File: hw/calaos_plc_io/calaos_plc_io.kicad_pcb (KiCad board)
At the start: 2 copper layers, 100.3 x 93.2 mm, 223 parts, among them P1 CONN_01X03, P2 CONN_01X06, P3 CONN_01X20, P4 CONN_01X20, P5 SERIAL_DBG, Q1 Q_NPN_BCE, Q10 Q_NPN_BCE, Q11 Q_NPN_BCE, Q12 Q_NPN_BCE, Q13 Q_NPN_BCE, Q14 Q_NPN_BCE, Q15 Q_NPN_BCE, Q16 Q_NPN_BCE, Q17 Q_NPN_BCE, Q18 Q_NPN_BCE, Q19 Q_NPN_BCE, Q2 Q_NPN_BCE, Q20 Q_NPN_BCE, Q3 Q_NPN_BCE, Q4 Q_NPN_BCE, Q5 Q_NPN_BCE, Q6 Q_NPN_BCE, Q7 Q_NPN_BCE, Q8 Q_NPN_BCE, Q9 Q_NPN_BCE, U1 LM7824CT, U10 LTV-847, U11 LTV-847, U12 LTV-847, U13 LTV-847, U14 LTV-847, U15 LTV-847, U16 LTV-847, U2 LM7805CT, U3 LTV-847, U4 LD1117S33TR, U5 MAX485, U6 STM32F030K6, U7 PCA9505, U8 LTV-847, U9 LTV-847, Y1 8MHz

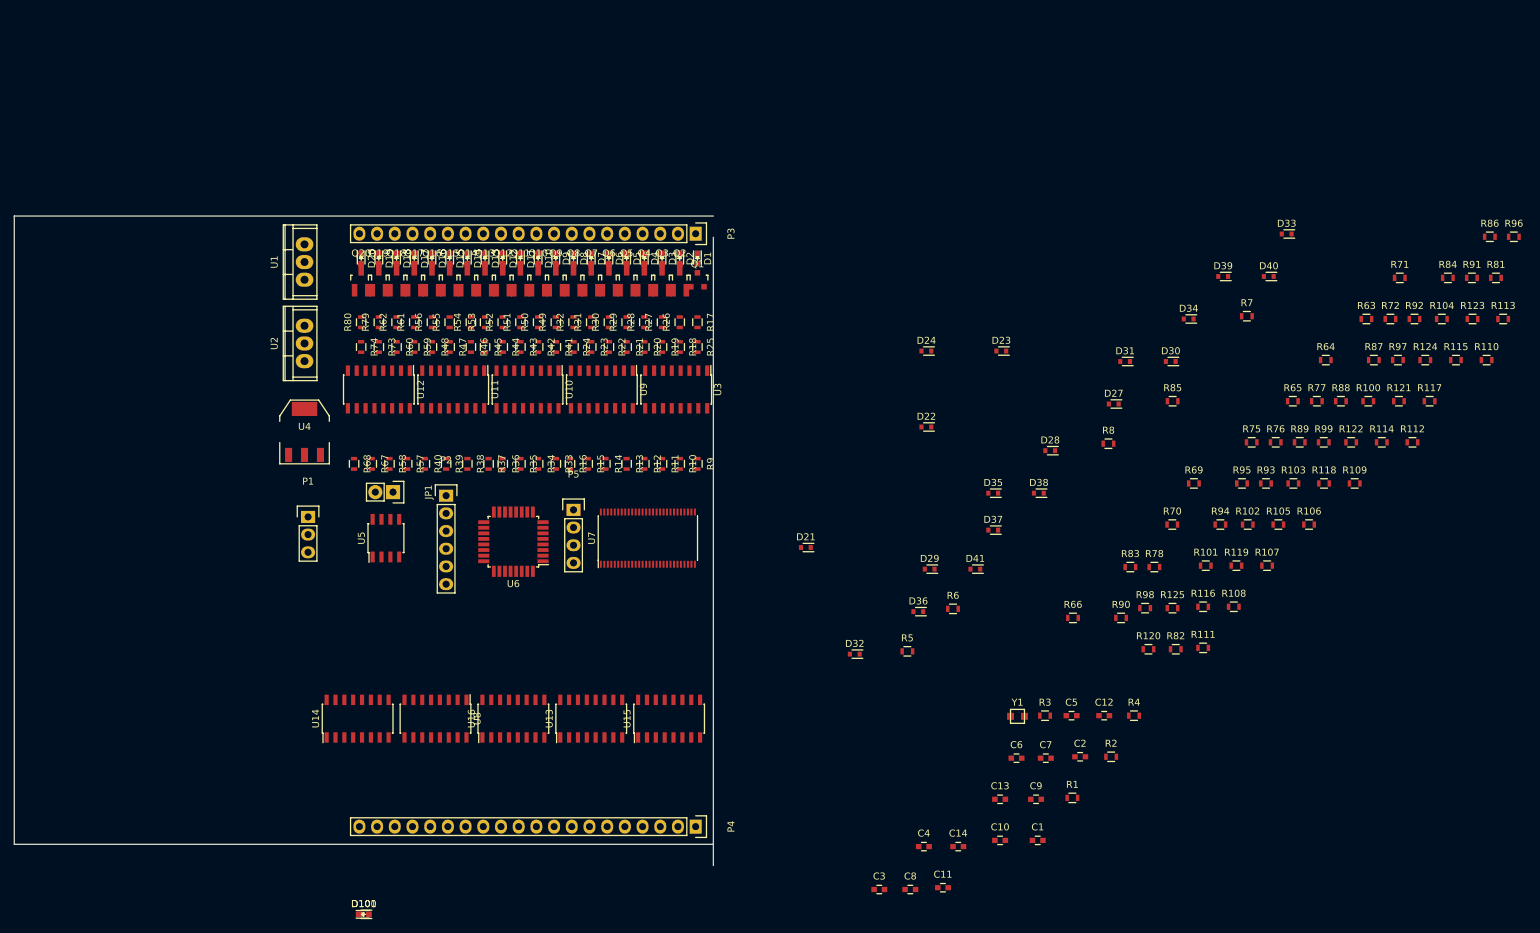
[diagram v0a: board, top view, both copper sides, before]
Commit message: Add pcb with placement of components
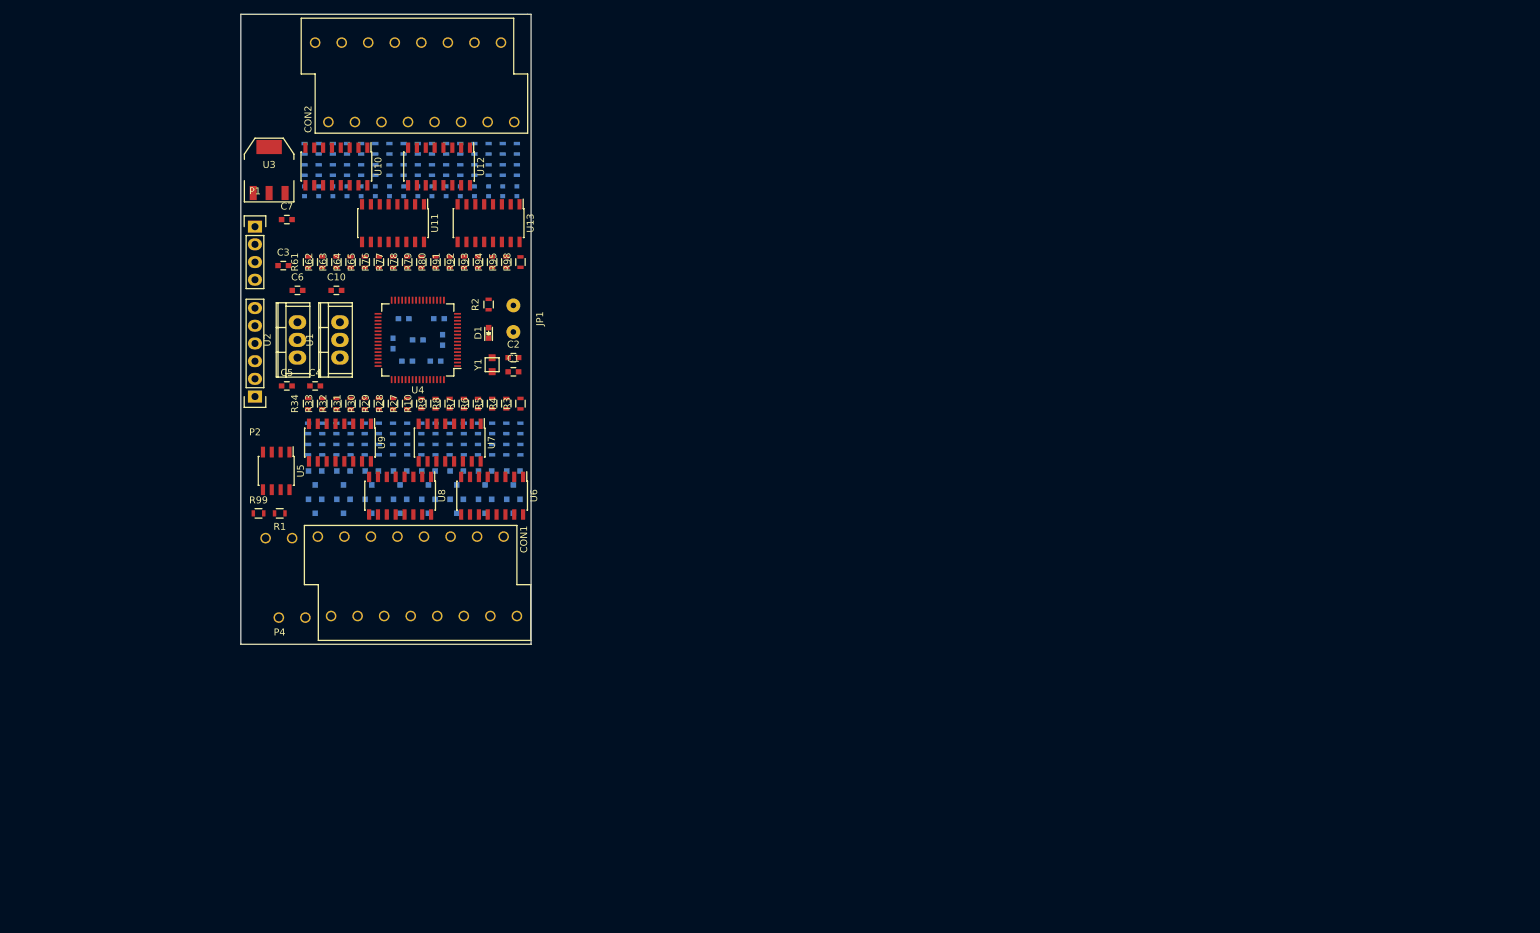
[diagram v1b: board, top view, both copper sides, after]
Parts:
- removed D10, D100, D11, D12, D13, D14, D15, D16, D17, D2, D3, D4, D5, D6, D7, D8, D9: LED, LEDs:LED-0603
- removed D101, D34, D35, D36, D37, D38, D39, D40, D41: TVS 3v3, Diodes_SMD:SOD-523
- removed P3: CONN_01X20, Pin_Headers:Pin_Header_Straight_1x20
- removed P5: SERIAL_DBG, Pin_Headers:Pin_Header_Straight_1x04
- removed Q17, Q18, Q19, Q20: Q_NPN_BCE, Housings_SOT-23_SOT-143_TSOT-6:SOT-23_Handsoldering
- removed R100, R101, R102, R103, R104, R105, R111, R112, R113, R114, R115, R116, R117, R118, R119, R120: 390, Resistors_SMD:R_0603
- removed R106, R107, R108, R109, R110, R121, R122, R123, R124, R125: 10k, Resistors_SMD:R_0603
- removed U14, U15, U16: LTV-847, Housings_SOIC:SOIC-16_3.9x9.9mm_Pitch1.27mm
- added C15: 100nF, Capacitors_SMD:C_0603, B.Cu at (149.4, 94.0)
- added CON1: TerminalBlock, plc:Terminalblock_1708084, F.Cu at (163.6, 133.6)
- added CON2: TerminalBlock, plc:Terminalblock_1708084, F.Cu at (134.6, 51.3)
- added D25: TVS 3v3, Diodes_SMD:SOD-523, B.Cu at (147.3, 72.6)
- added D26: TVS 3v3, Diodes_SMD:SOD-523, B.Cu at (149.4, 72.6)
- C1, C2: value 0.33uF -> 20pF
- C10: value 100nF -> 10uF
- C11, C12, C13, C14, C9, D21, D22, D23, D24, D27, D28, D29, D30, D31, D32, D33, Q1, R17, R18, R19, R20, R21, R22, R23, R24, R25, R26, R41, R42, R43, R44, R45, R46, R47, R48, R49, R50, R66, R69, R70, R71, R72, R81, R82, R83, R84, R85, R86, R87, R88, R89, R90, R96, R97: moved to B.Cu
- C3, C4: value 0.1uF -> 0.33uF
- C5, C6: value 20pF -> 0.1uF
- C8: value 10uF -> 100nF; moved to B.Cu
- D18, D19, D20: value LED -> TVS 3v3; footprint LEDs:LED-0603 -> Diodes_SMD:SOD-523; moved to B.Cu
- JP1: value JUMPER -> Jumper_NO_Small; footprint Pin_Headers:Pin_Header_Straight_1x02 -> Wire_Pads:SolderWirePad_2x_0-8mmDrill
- P1: value CONN_01X03 -> SERIAL_DBG; footprint Pin_Headers:Pin_Header_Straight_1x03 -> Pin_Headers:Pin_Header_Straight_1x04
- P4: value CONN_01X20 -> CONN_01X04; footprint Pin_Headers:Pin_Header_Straight_1x20 -> plc:Terminalbloc_1726040
- Q10, Q11, Q12, Q13, Q14, Q15, Q16, Q2, Q3, Q4, Q5, Q6, Q7, Q8, Q9: footprint Housings_SOT-23_SOT-143_TSOT-6:SOT-23_Handsoldering -> Housings_SOT-23_SOT-143_TSOT-6:SOT-23; moved to B.Cu
- R1: value 120 -> 1k
- R11, R12, R13, R14, R15, R16, R35, R36, R37, R38, R39, R40: value 220 -> 10k; moved to B.Cu
- R2: value 10k -> 510
- R27, R28, R29, R30, R31, R32, R7, R8: value 10k -> 220
- R3, R4: value 510 -> 220
- R5, R6: value 390 -> 220
- R51, R52, R53, R54, R55, R56, R59, R60, R73, R74, R75: value 10k -> 390; moved to B.Cu
- R57, R58, R67, R68: value 220 -> 390; moved to B.Cu
- R63, R64, R65, R98: value 390 -> 10k
- R99: value 390 -> 120
- U3: value LTV-847 -> LD1117S33TR; footprint Housings_SOIC:SOIC-16_3.9x9.9mm_Pitch1.27mm -> TO_SOT_Packages_SMD:SOT-223
- U4: value LD1117S33TR -> STM32F105R8; footprint TO_SOT_Packages_SMD:SOT-223 -> Housings_QFP:LQFP-64_10x10mm_Pitch0.5mm
- U5: value MAX485 -> MCP2551-I/SN
- U6: value STM32F030K6 -> LTV-847; footprint Housings_QFP:TQFP-32_7x7mm_Pitch0.8mm -> Housings_SOIC:SOIC-16_3.9x9.9mm_Pitch1.27mm
- U7: value PCA9505 -> LTV-847; footprint Housings_SSOP:TSSOP-56_6.1x14mm_Pitch0.5mm -> Housings_SOIC:SOIC-16_3.9x9.9mm_Pitch1.27mm
- moved R99 153.2 mm to (126.5, 118.9)
- moved R81 151.8 mm to (153.4, 66.5), turned to 270 degrees
- moved R86 150.1 mm to (153.4, 69.6), turned to 270 degrees
- moved R63 148.1 mm to (137.7, 82.8), turned to 90 degrees
- moved R71 147.8 mm to (143.3, 69.6), turned to 270 degrees
- moved R91 146.7 mm to (153.9, 82.8), turned to 90 degrees
- moved R72 145.2 mm to (145.3, 69.6), turned to 270 degrees
- moved R96 143.6 mm to (163.6, 66.5), turned to 270 degrees
- moved R64 140.7 mm to (139.7, 82.8), turned to 90 degrees
- moved R84 138.9 mm to (159.5, 66.5), turned to 270 degrees
- moved R92 136.7 mm to (156.0, 82.8), turned to 90 degrees
- moved R65 134.7 mm to (141.7, 82.8), turned to 90 degrees
- moved R77 134.1 mm to (145.8, 82.8), turned to 90 degrees
- moved R87 133.9 mm to (155.4, 69.6), turned to 270 degrees
- moved C7 133.6 mm to (130.6, 76.7)
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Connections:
- C1 pad 1: VIN -> Net-(C1-Pad1)
- C2 pad 1: VIN -> Net-(C2-Pad1)
- C3 pad 1: +24V -> VIN
- C4 pad 1: +5V -> VIN
- C5 pad 1: Net-(C5-Pad1) -> +24V
- C6 pad 1: Net-(C6-Pad1) -> +5V
- D18 pad 1: GND -> Net-(D18-Pad1)
- D18 pad 2: Net-(D18-Pad2) -> GNDREF
- D19 pad 1: GND -> Net-(D19-Pad1)
- D19 pad 2: Net-(D19-Pad2) -> GNDREF
- D20 pad 1: GND -> Net-(D20-Pad1)
- D20 pad 2: Net-(D20-Pad2) -> GNDREF
- P1 pad 1: /A -> GND
- P1 pad 2: /B -> DBG_TX
- P1 pad 3: GND -> DBG_RX
- P4 pad 1: /Inputs-1/DI_01 -> +24V
- P4 pad 2: /Inputs-1/DI_02 -> /CANH
- P4 pad 3: /Inputs-1/DI_03 -> /CANL
- P4 pad 4: /Inputs-1/DI_04 -> GND
- R1 pad 1: Net-(JP1-Pad1) -> Net-(R1-Pad1)
- R1 pad 2: /A -> GND
- R10 pad 2: /Inputs-1/O_1 -> /Inputs-1/O_7
- R11 pad 1: Net-(R11-Pad1) -> +24V
- R11 pad 2: /Inputs-1/O_2 -> Net-(Q1-Pad1)
- R12 pad 1: Net-(R12-Pad1) -> +24V
- R12 pad 2: /Inputs-1/O_3 -> Net-(Q2-Pad1)
- R13 pad 1: Net-(R13-Pad1) -> +24V
- R13 pad 2: /Inputs-1/O_4 -> Net-(Q3-Pad1)
- R14 pad 1: Net-(R14-Pad1) -> +24V
- R14 pad 2: /Inputs-1/O_5 -> Net-(Q4-Pad1)
- R15 pad 1: Net-(R15-Pad1) -> +24V
- R15 pad 2: /Inputs-1/O_6 -> Net-(Q5-Pad1)
- R16 pad 1: Net-(R16-Pad1) -> +24V
- R16 pad 2: /Inputs-1/O_7 -> Net-(Q6-Pad1)
- R17 pad 2: Net-(Q1-Pad1) -> Net-(Q7-Pad1)
- R18 pad 2: Net-(Q2-Pad1) -> Net-(Q8-Pad1)
- R19 pad 2: Net-(Q3-Pad1) -> /Inputs-1/DO_01
- R2 pad 1: +3V3 -> Net-(R2-Pad1)
- R2 pad 2: Net-(R2-Pad2) -> Net-(D1-Pad2)
- R20 pad 2: Net-(Q4-Pad1) -> /Inputs-1/DO_02
- R21 pad 2: Net-(Q5-Pad1) -> /Inputs-1/DO_03
- R22 pad 2: Net-(Q6-Pad1) -> /Inputs-1/DO_04
- R23 pad 2: Net-(Q7-Pad1) -> /Inputs-1/DO_05
- R24 pad 2: Net-(Q8-Pad1) -> /Inputs-1/DO_06
- R25 pad 2: /Inputs-1/DO_01 -> /Inputs-1/DO_07
- R26 pad 2: /Inputs-1/DO_02 -> /Inputs-1/DO_08
- R27 pad 1: +24V -> Net-(R27-Pad1)
- R27 pad 2: /Inputs-1/DO_03 -> /Inputs-1/O_8
- R28 pad 1: +24V -> Net-(R28-Pad1)
- R28 pad 2: /Inputs-1/DO_04 -> /Inputs-1/O_9
- R29 pad 1: +24V -> Net-(R29-Pad1)
- R29 pad 2: /Inputs-1/DO_05 -> /Inputs-1/O_10
- R3 pad 1: Net-(R2-Pad2) -> Net-(R3-Pad1)
- R3 pad 2: GND -> /Inputs-1/O_0
- R30 pad 1: +24V -> Net-(R30-Pad1)
- R30 pad 2: /Inputs-1/DO_06 -> /Inputs-1/O_11
- R31 pad 1: +24V -> Net-(R31-Pad1)
- R31 pad 2: /Inputs-1/DO_07 -> /Inputs-1/O_12
- R32 pad 1: +24V -> Net-(R32-Pad1)
- R32 pad 2: /Inputs-1/DO_08 -> /Inputs-1/O_13
- R33 pad 2: /Inputs-1/O_8 -> /Inputs-1/O_14
- R34 pad 2: /Inputs-1/O_9 -> /Inputs-1/O_15
- R35 pad 1: Net-(R35-Pad1) -> +24V
- R35 pad 2: /Inputs-1/O_10 -> Net-(Q9-Pad1)
- R36 pad 1: Net-(R36-Pad1) -> +24V
- R36 pad 2: /Inputs-1/O_11 -> Net-(Q10-Pad1)
- R37 pad 1: Net-(R37-Pad1) -> +24V
- R37 pad 2: /Inputs-1/O_12 -> Net-(Q11-Pad1)
- R38 pad 1: Net-(R38-Pad1) -> +24V
- R38 pad 2: /Inputs-1/O_13 -> Net-(Q12-Pad1)
- R39 pad 1: Net-(R39-Pad1) -> +24V
- R39 pad 2: /Inputs-1/O_14 -> Net-(Q13-Pad1)
- R4 pad 2: Net-(D100-Pad2) -> /Inputs-1/O_1
- R40 pad 1: Net-(R40-Pad1) -> +24V
- R40 pad 2: /Inputs-1/O_15 -> Net-(Q14-Pad1)
- R41 pad 2: Net-(Q9-Pad1) -> Net-(Q15-Pad1)
- R42 pad 2: Net-(Q10-Pad1) -> Net-(Q16-Pad1)
- R43 pad 2: Net-(Q11-Pad1) -> /Inputs-1/DO_09
- R44 pad 2: Net-(Q12-Pad1) -> /Inputs-1/DO_10
- R45 pad 2: Net-(Q13-Pad1) -> /Inputs-1/DO_11
- R46 pad 2: Net-(Q14-Pad1) -> /Inputs-1/DO_12
- R47 pad 2: Net-(Q15-Pad1) -> /Inputs-1/DO_13
- R48 pad 2: Net-(Q16-Pad1) -> /Inputs-1/DO_14
- R49 pad 2: /Inputs-1/DO_09 -> /Inputs-1/DO_15
- R5 pad 1: Net-(D21-Pad1) -> Net-(R5-Pad1)
- R5 pad 2: /Inputs-1/DI_01 -> /Inputs-1/O_2
- R50 pad 2: /Inputs-1/DO_10 -> /Inputs-1/DO_16
- R51 pad 1: +24V -> Net-(D18-Pad1)
- R51 pad 2: /Inputs-1/DO_11 -> /Inputs-1/DI_01
- R52 pad 1: +24V -> Net-(D19-Pad1)
- R52 pad 2: /Inputs-1/DO_12 -> /Inputs-1/DI_02
- R53 pad 1: +24V -> Net-(D20-Pad1)
- R53 pad 2: /Inputs-1/DO_13 -> /Inputs-1/DI_03
- R54 pad 1: +24V -> Net-(D21-Pad1)
- R54 pad 2: /Inputs-1/DO_14 -> /Inputs-1/DI_04
- R55 pad 1: +24V -> Net-(D22-Pad1)
- R55 pad 2: /Inputs-1/DO_15 -> /Inputs-1/DI_05
- R56 pad 1: +24V -> Net-(R56-Pad1)
- R56 pad 2: /Inputs-1/DO_16 -> Net-(D18-Pad1)
- R57 pad 2: /Inputs-1/O_16 -> Net-(D19-Pad1)
- R58 pad 2: /Inputs-1/O_17 -> Net-(D20-Pad1)
- R59 pad 1: +24V -> Net-(R59-Pad1)
- R59 pad 2: Net-(Q17-Pad1) -> Net-(D21-Pad1)
- R6 pad 2: Net-(D21-Pad1) -> /Inputs-1/O_3
- R60 pad 1: +24V -> Net-(R60-Pad1)
- R60 pad 2: Net-(Q18-Pad1) -> Net-(D22-Pad1)
- R61 pad 1: +24V -> +5V
- R61 pad 2: /Inputs-1/DO_17 -> /Inputs-1/I_0
- R62 pad 1: +24V -> +5V
- R62 pad 2: /Inputs-1/DO_18 -> /Inputs-1/I_1
- R63 pad 1: Net-(D101-Pad1) -> +5V
- R63 pad 2: /Inputs-1/DI_02 -> /Inputs-1/I_2
- R64 pad 1: Net-(D22-Pad1) -> +5V
- R64 pad 2: /Inputs-1/DI_03 -> /Inputs-1/I_3
- R65 pad 1: Net-(D23-Pad1) -> +5V
- R65 pad 2: /Inputs-1/DI_04 -> /Inputs-1/I_4
- R66 pad 1: Net-(D24-Pad1) -> Net-(D23-Pad1)
- R66 pad 2: /Inputs-1/DI_05 -> /Inputs-1/DI_06
- R67 pad 1: Net-(R67-Pad1) -> Net-(D24-Pad1)
- R67 pad 2: /Inputs-1/O_18 -> /Inputs-1/DI_07
- R68 pad 1: Net-(R68-Pad1) -> Net-(D25-Pad1)
- R68 pad 2: /Inputs-1/O_19 -> /Inputs-1/DI_08
- R69 pad 1: Net-(R69-Pad1) -> Net-(D26-Pad1)
- R69 pad 2: Net-(D101-Pad1) -> /Inputs-1/DI_09
- R7 pad 1: +5V -> Net-(R7-Pad1)
- R7 pad 2: /Inputs-1/I_0 -> /Inputs-1/O_4
- R70 pad 1: Net-(R70-Pad1) -> Net-(D27-Pad1)
- R70 pad 2: Net-(D22-Pad1) -> /Inputs-1/DI_10
- R73 pad 1: +24V -> Net-(R73-Pad1)
- R73 pad 2: Net-(Q19-Pad1) -> Net-(D25-Pad1)
- R74 pad 1: +24V -> Net-(R74-Pad1)
- R74 pad 2: Net-(Q20-Pad1) -> Net-(D26-Pad1)
- R75 pad 1: +5V -> Net-(R75-Pad1)
- R75 pad 2: /Inputs-1/I_1 -> Net-(D27-Pad1)
- R76 pad 2: /Inputs-1/I_2 -> /Inputs-1/I_5
- R77 pad 2: /Inputs-1/I_3 -> /Inputs-1/I_6
- R78 pad 2: /Inputs-1/I_4 -> /Inputs-1/I_7
- R79 pad 1: +24V -> +5V
- R79 pad 2: /Inputs-1/DO_19 -> /Inputs-1/I_8
- R8 pad 1: +5V -> Net-(R8-Pad1)
- R8 pad 2: Net-(R8-Pad2) -> /Inputs-1/O_5
- R80 pad 1: +24V -> +5V
- R80 pad 2: /Inputs-1/DO_20 -> /Inputs-1/I_9
- R81 pad 1: Net-(D27-Pad1) -> Net-(D28-Pad1)
- R81 pad 2: /Inputs-1/DI_06 -> /Inputs-1/DI_11
- R82 pad 1: Net-(D28-Pad1) -> Net-(D29-Pad1)
- R82 pad 2: /Inputs-1/DI_07 -> /Inputs-1/DI_12
- R83 pad 1: Net-(D29-Pad1) -> Net-(D30-Pad1)
- R83 pad 2: /Inputs-1/DI_08 -> /Inputs-1/DI_13
- R84 pad 1: Net-(D30-Pad1) -> Net-(D31-Pad1)
- R84 pad 2: /Inputs-1/DI_09 -> /Inputs-1/DI_14
- R85 pad 1: Net-(D31-Pad1) -> Net-(D32-Pad1)
- R85 pad 2: /Inputs-1/DI_10 -> /Inputs-1/DI_15
- R86 pad 2: Net-(D27-Pad1) -> Net-(D28-Pad1)
- R87 pad 2: Net-(D28-Pad1) -> Net-(D29-Pad1)
- R88 pad 2: Net-(D29-Pad1) -> Net-(D30-Pad1)
- R89 pad 2: Net-(D30-Pad1) -> Net-(D31-Pad1)
- R9 pad 2: /Inputs-1/O_0 -> /Inputs-1/O_6
- R90 pad 2: Net-(D31-Pad1) -> Net-(D32-Pad1)
- R91 pad 2: /Inputs-1/I_5 -> /Inputs-1/I_10
- R92 pad 2: /Inputs-1/I_6 -> /Inputs-1/I_11
- R93 pad 2: /Inputs-1/I_7 -> /Inputs-1/I_12
- R94 pad 2: /Inputs-1/I_8 -> /Inputs-1/I_13
- R95 pad 2: /Inputs-1/I_9 -> /Inputs-1/I_14
- R96 pad 1: Net-(D32-Pad1) -> Net-(D33-Pad1)
- R96 pad 2: /Inputs-1/DI_11 -> /Inputs-1/DI_16
- R97 pad 1: Net-(D33-Pad1) -> Net-(R97-Pad1)
- R97 pad 2: /Inputs-1/DI_12 -> Net-(D33-Pad1)
- R98 pad 1: Net-(D34-Pad1) -> +5V
- R98 pad 2: /Inputs-1/DI_13 -> /Inputs-1/I_15
- R99 pad 1: Net-(D35-Pad1) -> Net-(JP1-Pad1)
- R99 pad 2: /Inputs-1/DI_14 -> /CANL
- U10 pad 1: Net-(R33-Pad1) -> Net-(R56-Pad1)
- U10 pad 10: Net-(Q12-Pad1) -> /Inputs-1/I_3
- U10 pad 11: GNDREF -> GND
- U10 pad 12: Net-(Q11-Pad1) -> /Inputs-1/I_2
- U10 pad 13: GNDREF -> GND
- U10 pad 14: Net-(Q10-Pad1) -> /Inputs-1/I_1
- U10 pad 15: GNDREF -> GND
- U10 pad 16: Net-(Q9-Pad1) -> /Inputs-1/I_0
- U10 pad 2: Net-(D9-Pad2) -> GNDREF
- U10 pad 3: Net-(R34-Pad1) -> Net-(R57-Pad1)
- U10 pad 4: Net-(D10-Pad2) -> GNDREF
- U10 pad 5: Net-(R35-Pad1) -> Net-(R58-Pad1)
- U10 pad 6: Net-(D11-Pad2) -> GNDREF
- U10 pad 7: Net-(R36-Pad1) -> Net-(R59-Pad1)
- U10 pad 8: Net-(D12-Pad2) -> GNDREF
- U10 pad 9: GNDREF -> GND
- U11 pad 1: Net-(R37-Pad1) -> Net-(R60-Pad1)
- U11 pad 10: Net-(Q16-Pad1) -> /Inputs-1/I_7
- U11 pad 11: GNDREF -> GND
- U11 pad 12: Net-(Q15-Pad1) -> /Inputs-1/I_6
- U11 pad 13: GNDREF -> GND
- U11 pad 14: Net-(Q14-Pad1) -> /Inputs-1/I_5
- U11 pad 15: GNDREF -> GND
- U11 pad 16: Net-(Q13-Pad1) -> /Inputs-1/I_4
- U11 pad 2: Net-(D13-Pad2) -> GNDREF
- U11 pad 3: Net-(R38-Pad1) -> Net-(R71-Pad1)
- U11 pad 4: Net-(D14-Pad2) -> GNDREF
- U11 pad 5: Net-(R39-Pad1) -> Net-(R72-Pad1)
- U11 pad 6: Net-(D15-Pad2) -> GNDREF
- U11 pad 7: Net-(R40-Pad1) -> Net-(R73-Pad1)
- U11 pad 8: Net-(D16-Pad2) -> GNDREF
- U11 pad 9: GNDREF -> GND
- U12 pad 1: Net-(R57-Pad1) -> Net-(R74-Pad1)
- U12 pad 10: Net-(Q20-Pad1) -> /Inputs-1/I_11
- U12 pad 11: GNDREF -> GND
- U12 pad 12: Net-(Q19-Pad1) -> /Inputs-1/I_10
- U12 pad 13: GNDREF -> GND
- U12 pad 14: Net-(Q18-Pad1) -> /Inputs-1/I_9
- U12 pad 15: GNDREF -> GND
- U12 pad 16: Net-(Q17-Pad1) -> /Inputs-1/I_8
- U12 pad 2: Net-(D17-Pad2) -> GNDREF
- U12 pad 3: Net-(R58-Pad1) -> Net-(R75-Pad1)
- U12 pad 4: Net-(D18-Pad2) -> GNDREF
- U12 pad 5: Net-(R67-Pad1) -> Net-(R86-Pad1)
- U12 pad 6: Net-(D19-Pad2) -> GNDREF
- U12 pad 7: Net-(R68-Pad1) -> Net-(R87-Pad1)
- U12 pad 8: Net-(D20-Pad2) -> GNDREF
- U12 pad 9: GNDREF -> GND
- U13 pad 1: Net-(R72-Pad1) -> Net-(R88-Pad1)
- U13 pad 10: /Inputs-1/I_7 -> /Inputs-1/I_15
- U13 pad 12: /Inputs-1/I_6 -> /Inputs-1/I_14
- U13 pad 14: /Inputs-1/I_5 -> /Inputs-1/I_13
- U13 pad 16: /Inputs-1/I_4 -> /Inputs-1/I_12
- U13 pad 3: Net-(R86-Pad1) -> Net-(R89-Pad1)
- U13 pad 5: Net-(R87-Pad1) -> Net-(R90-Pad1)
- U13 pad 7: Net-(R88-Pad1) -> Net-(R97-Pad1)
- U3 pad 1: Net-(R9-Pad1) -> GND
- U3 pad 2: Net-(D1-Pad2) -> +3V3
- U3 pad 3: Net-(R10-Pad1) -> +5V
- U3 pad 4: Net-(D2-Pad2) -> (no net)
- U4 pad 1: GND -> (no net)
- U4 pad 2: +3V3 -> /Inputs-1/O_13
- U4 pad 3: +5V -> /Inputs-1/O_14
- U4 pad 4: (no net) -> /Inputs-1/O_15
- U5 pad 1: RX -> CAN_TX
- U5 pad 2: CTS -> GND
- U5 pad 3: CTS -> +3V3
- U5 pad 4: TX -> CAN_RX
- U5 pad 5: GND -> (no net)
- U5 pad 6: /A -> /CANL
- U5 pad 7: /B -> /CANH
- U5 pad 8: +3V3 -> Net-(R1-Pad1)
- U6 pad 1: +3V3 -> Net-(R3-Pad1)
- U6 pad 10: (no net) -> Net-(Q4-Pad1)
- U6 pad 11: (no net) -> GNDREF
- U6 pad 12: (no net) -> Net-(Q3-Pad1)
- U6 pad 13: (no net) -> GNDREF
- U6 pad 14: INT -> Net-(Q2-Pad1)
- U6 pad 15: (no net) -> GNDREF
- U6 pad 16: GND -> Net-(Q1-Pad1)
- U6 pad 2: Net-(C5-Pad1) -> GND
- U6 pad 3: Net-(C6-Pad1) -> Net-(R4-Pad1)
- U6 pad 4: NRST -> GND
- U6 pad 5: +3V3 -> Net-(R5-Pad1)
- U6 pad 6: Net-(R2-Pad2) -> GND
- U6 pad 7: (no net) -> Net-(R6-Pad1)
- U6 pad 8: DBG_TX -> GND
- U6 pad 9: DBG_RX -> GNDREF
- U7 pad 1: SCA -> Net-(R7-Pad1)
- U7 pad 10: /Inputs-1/I_6 -> Net-(Q8-Pad1)
- U7 pad 11: GND -> GNDREF
- U7 pad 12: /Inputs-1/I_7 -> Net-(Q7-Pad1)
- U7 pad 13: /Inputs-1/I_8 -> GNDREF
- U7 pad 14: /Inputs-1/I_9 -> Net-(Q6-Pad1)
- U7 pad 15: /Inputs-1/I_10 -> GNDREF
- U7 pad 16: /Inputs-1/I_11 -> Net-(Q5-Pad1)
- U7 pad 2: SCL -> GND
- U7 pad 3: /Inputs-1/I_0 -> Net-(R8-Pad1)
- U7 pad 4: /Inputs-1/I_1 -> GND
- U7 pad 5: /Inputs-1/I_2 -> Net-(R9-Pad1)
- U7 pad 7: /Inputs-1/I_3 -> Net-(R10-Pad1)
- U7 pad 8: /Inputs-1/I_4 -> GND
- U7 pad 9: /Inputs-1/I_5 -> GNDREF
- U8 pad 1: Net-(R6-Pad1) -> Net-(R27-Pad1)
- U8 pad 10: /Inputs-1/I_3 -> Net-(Q12-Pad1)
- U8 pad 11: GND -> GNDREF
- U8 pad 12: /Inputs-1/I_2 -> Net-(Q11-Pad1)
- U8 pad 13: GND -> GNDREF
- U8 pad 14: /Inputs-1/I_1 -> Net-(Q10-Pad1)
- U8 pad 15: GND -> GNDREF
- U8 pad 16: /Inputs-1/I_0 -> Net-(Q9-Pad1)
- U8 pad 2: GNDREF -> GND
- U8 pad 3: Net-(R69-Pad1) -> Net-(R28-Pad1)
- U8 pad 4: GNDREF -> GND
- U8 pad 5: Net-(R70-Pad1) -> Net-(R29-Pad1)
- U8 pad 6: GNDREF -> GND
- U8 pad 7: Net-(R71-Pad1) -> Net-(R30-Pad1)
- U8 pad 8: GNDREF -> GND
- U8 pad 9: GND -> GNDREF
- U9 pad 1: Net-(R13-Pad1) -> Net-(R31-Pad1)
- U9 pad 10: Net-(Q8-Pad1) -> Net-(Q16-Pad1)
- U9 pad 12: Net-(Q7-Pad1) -> Net-(Q15-Pad1)
- U9 pad 14: Net-(Q6-Pad1) -> Net-(Q14-Pad1)
- U9 pad 16: Net-(Q5-Pad1) -> Net-(Q13-Pad1)
- U9 pad 2: Net-(D5-Pad2) -> GND
- U9 pad 3: Net-(R14-Pad1) -> Net-(R32-Pad1)
- U9 pad 4: Net-(D6-Pad2) -> GND
- U9 pad 5: Net-(R15-Pad1) -> Net-(R33-Pad1)
- U9 pad 6: Net-(D7-Pad2) -> GND
- U9 pad 7: Net-(R16-Pad1) -> Net-(R34-Pad1)
- U9 pad 8: Net-(D8-Pad2) -> GND
- Y1 pad 1: Net-(C5-Pad1) -> Net-(C1-Pad1)
- Y1 pad 2: Net-(C6-Pad1) -> Net-(C2-Pad1)
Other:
- board size 100.3 x 93.2 mm -> 41.7 x 90.4 mm

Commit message: Update schematics and pcb
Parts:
- removed U2: LM7805CT, Power_Integrations:TO-220
- added 4A1: Fuse, Fuse_Holders_and_Fuses:Fuse_SMD1206_Reflow, F.Cu at (128.0, 71.6)
- added C16: 10uF, Capacitors_SMD:C_0603, F.Cu at (128.0, 86.4)
- added C17: 47uF, Capacitors_SMD:C_0603, F.Cu at (129.0, 107.2)
- added C18: 0.01uF, Capacitors_SMD:C_0603, F.Cu at (125.0, 98.0)
- added D2: D_Schottky, Diodes_SMD:SOD-523, F.Cu at (128.0, 67.6)
- added D3: TVS, Diodes_SMD:SOD-523, F.Cu at (128.0, 75.2)
- added D4: B340A-13-F, Diodes_SMD:SOD-523, F.Cu at (130.0, 98.0)
- added L1: 68uH, Inductors:SELF-WE-TPC_M, F.Cu at (126.0, 102.6)
- added P3: CONN_01X04, plc:Terminalbloc_1726040, F.Cu at (119.9, 122.4)
- added P5: CONN_01X04, plc:Terminalbloc_1726040, F.Cu at (127.5, 51.3)
- added P6: CONN_01X04, plc:Terminalbloc_1726040, F.Cu at (120.4, 51.3)
- added P7: CONN_02X06, Pin_Headers:Pin_Header_Straight_2x06, F.Cu at (119.9, 79.8)
- added R100: 10K, Resistors_SMD:R_0603, F.Cu at (130.6, 100.6)
- added R101: 3.24K, Resistors_SMD:R_0603, F.Cu at (130.6, 104.1)
- added R102: R, Resistors_SMD:R_0603, F.Cu at (160.0, 99.6)
- added R103: R, Resistors_SMD:R_0603, F.Cu at (163.6, 99.6)
- C3, C4: value 0.33uF -> 0.1uF
- C5, C6: value 0.1uF -> 10uF
- U1: value LM7824CT -> TPS5420D; footprint Power_Integrations:TO-220 -> Housings_SOIC:SOIC-8_3.9x4.9mm_Pitch1.27mm
- Y1: footprint Crystals_Oscillators_SMD:crystal_FA238-TSX3225 -> Crystals:Crystal_FOX-FE_SMD
- moved U3 25.8 mm to (137.7, 93.5)
- moved C7 23.9 mm to (137.7, 99.6), turned to 180 degrees
- moved C4 22.3 mm to (128.0, 79.2)
- moved C5 19.5 mm to (128.0, 81.3)
- moved P1 11.8 mm to (119.9, 67.6)
- moved U1 9.77 mm to (128.5, 92.5)
- moved P2 9.37 mm to (119.9, 109.2)
- moved C3 6.43 mm to (128.0, 77.2)
- moved C6 5.08 mm to (128.0, 83.8)
- moved D1 5.08 mm to (159.5, 87.9), turned to 180 degrees
- moved Y1 4.10 mm to (159.5, 93.5), turned to 270 degrees
- moved R2 3.05 mm to (159.5, 85.9), turned to 0 degrees
- moved C15 1.61 mm to (150.9, 93.5)
- moved C9 1.61 mm to (154.4, 93.5)
- moved C12 1.52 mm to (153.4, 97.0)
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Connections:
- C3 pad 1: VIN -> +24V
- C4 pad 1: VIN -> +24V
- C6 pad 1: +5V -> +24V
- R61 pad 2: /Inputs-1/I_0 -> /Inputs-1/I_1
- R62 pad 2: /Inputs-1/I_1 -> /Inputs-1/I_2
- R63 pad 2: /Inputs-1/I_2 -> /Inputs-1/I_3
- R64 pad 2: /Inputs-1/I_3 -> /Inputs-1/I_4
- R65 pad 2: /Inputs-1/I_4 -> /Inputs-1/I_5
- R76 pad 2: /Inputs-1/I_5 -> /Inputs-1/I_6
- R77 pad 2: /Inputs-1/I_6 -> /Inputs-1/I_7
- R78 pad 2: /Inputs-1/I_7 -> /Inputs-1/I_8
- R79 pad 2: /Inputs-1/I_8 -> /Inputs-1/I_9
- R80 pad 2: /Inputs-1/I_9 -> /Inputs-1/I_10
- R91 pad 2: /Inputs-1/I_10 -> /Inputs-1/I_11
- R92 pad 2: /Inputs-1/I_11 -> /Inputs-1/I_12
- R93 pad 2: /Inputs-1/I_12 -> /Inputs-1/I_13
- R94 pad 2: /Inputs-1/I_13 -> /Inputs-1/I_14
- R95 pad 2: /Inputs-1/I_14 -> /Inputs-1/I_15
- R98 pad 2: /Inputs-1/I_15 -> /Inputs-1/I_16
- U1 pad 1: VIN -> Net-(C18-Pad2)
- U1 pad 2: GND -> (no net)
- U1 pad 3: +24V -> (no net)
- U10 pad 10: /Inputs-1/I_3 -> /Inputs-1/I_4
- U10 pad 12: /Inputs-1/I_2 -> /Inputs-1/I_3
- U10 pad 14: /Inputs-1/I_1 -> /Inputs-1/I_2
- U10 pad 16: /Inputs-1/I_0 -> /Inputs-1/I_1
- U11 pad 10: /Inputs-1/I_7 -> /Inputs-1/I_8
- U11 pad 12: /Inputs-1/I_6 -> /Inputs-1/I_7
- U11 pad 14: /Inputs-1/I_5 -> /Inputs-1/I_6
- U11 pad 16: /Inputs-1/I_4 -> /Inputs-1/I_5
- U12 pad 10: /Inputs-1/I_11 -> /Inputs-1/I_12
- U12 pad 12: /Inputs-1/I_10 -> /Inputs-1/I_11
- U12 pad 14: /Inputs-1/I_9 -> /Inputs-1/I_10
- U12 pad 16: /Inputs-1/I_8 -> /Inputs-1/I_9
- U13 pad 10: /Inputs-1/I_15 -> /Inputs-1/I_16
- U13 pad 12: /Inputs-1/I_14 -> /Inputs-1/I_15
- U13 pad 14: /Inputs-1/I_13 -> /Inputs-1/I_14
- U13 pad 16: /Inputs-1/I_12 -> /Inputs-1/I_13
- U4 pad 14: (no net) -> PA0
- U4 pad 15: (no net) -> Net-(R102-Pad2)
- U4 pad 16: (no net) -> PA2
- U4 pad 17: (no net) -> PA3
- U4 pad 20: (no net) -> PA4
- U4 pad 21: (no net) -> PA5
- U4 pad 22: (no net) -> PA6
- U4 pad 23: (no net) -> PA7
- U4 pad 26: (no net) -> /Inputs-1/I_1
- U4 pad 27: (no net) -> /Inputs-1/I_2
- U4 pad 28: (no net) -> /Inputs-1/I_3
- U4 pad 29: (no net) -> /Inputs-1/I_11
- U4 pad 30: (no net) -> /Inputs-1/I_12
- U4 pad 33: (no net) -> /Inputs-1/I_13
- U4 pad 34: (no net) -> /Inputs-1/I_14
- U4 pad 35: (no net) -> /Inputs-1/I_15
- U4 pad 36: (no net) -> /Inputs-1/I_16
- U4 pad 41: (no net) -> PA8
- U4 pad 54: (no net) -> PD2
- U4 pad 55: (no net) -> /Inputs-1/I_4
- U4 pad 56: (no net) -> /Inputs-1/I_5
- U4 pad 57: (no net) -> /Inputs-1/I_6
- U4 pad 58: (no net) -> /Inputs-1/I_7
- U4 pad 59: (no net) -> /Inputs-1/I_8
- U4 pad 61: (no net) -> /Inputs-1/I_9
- U4 pad 62: (no net) -> /Inputs-1/I_10
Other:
- board size 41.7 x 90.4 mm -> 47.8 x 89.4 mm
